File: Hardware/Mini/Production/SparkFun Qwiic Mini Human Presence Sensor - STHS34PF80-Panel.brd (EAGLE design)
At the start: 175 x 93 mm, 1410 parts, among them J1 Qwiic, J10 Qwiic, J100 Qwiic, J101 Qwiic, J103 Qwiic, J104 Qwiic, J106 Qwiic, J107 Qwiic, J11 Qwiic, J13 Qwiic, J14 Qwiic, J16 Qwiic, J17 Qwiic, J19 Qwiic, J2 Qwiic, J20 Qwiic, J22 Qwiic, J23 Qwiic, J25 Qwiic, J26 Qwiic, J28 Qwiic, J29 Qwiic, J31 Qwiic, J32 Qwiic, J34 Qwiic, J35 Qwiic, J37 Qwiic, J38 Qwiic, J4 Qwiic, J40 Qwiic, J41 Qwiic, J43 Qwiic, J44 Qwiic, J46 Qwiic, J47 Qwiic, J49 Qwiic, J5 Qwiic, J50 Qwiic, J52 Qwiic, J53 Qwiic, J55 Qwiic, J56 Qwiic, J58 Qwiic, J59 Qwiic, J61 Qwiic, J62 Qwiic, J64 Qwiic, J65 Qwiic, J67 Qwiic, J68 Qwiic, J7 Qwiic, J70 Qwiic, J71 Qwiic, J73 Qwiic, J74 Qwiic, J76 Qwiic, J77 Qwiic, J79 Qwiic, J8 Qwiic, J80 Qwiic, J82 Qwiic, J83 Qwiic, J85 Qwiic, J86 Qwiic, J88 Qwiic, J89 Qwiic, J91 Qwiic, J92 Qwiic, J94 Qwiic, J95 Qwiic, J97 Qwiic, J98 Qwiic, U1 STHS34PF80, U10 STHS34PF80, U11 STHS34PF80, U12 STHS34PF80, U13 STHS34PF80, U14 STHS34PF80, U15 STHS34PF80, U16 STHS34PF80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

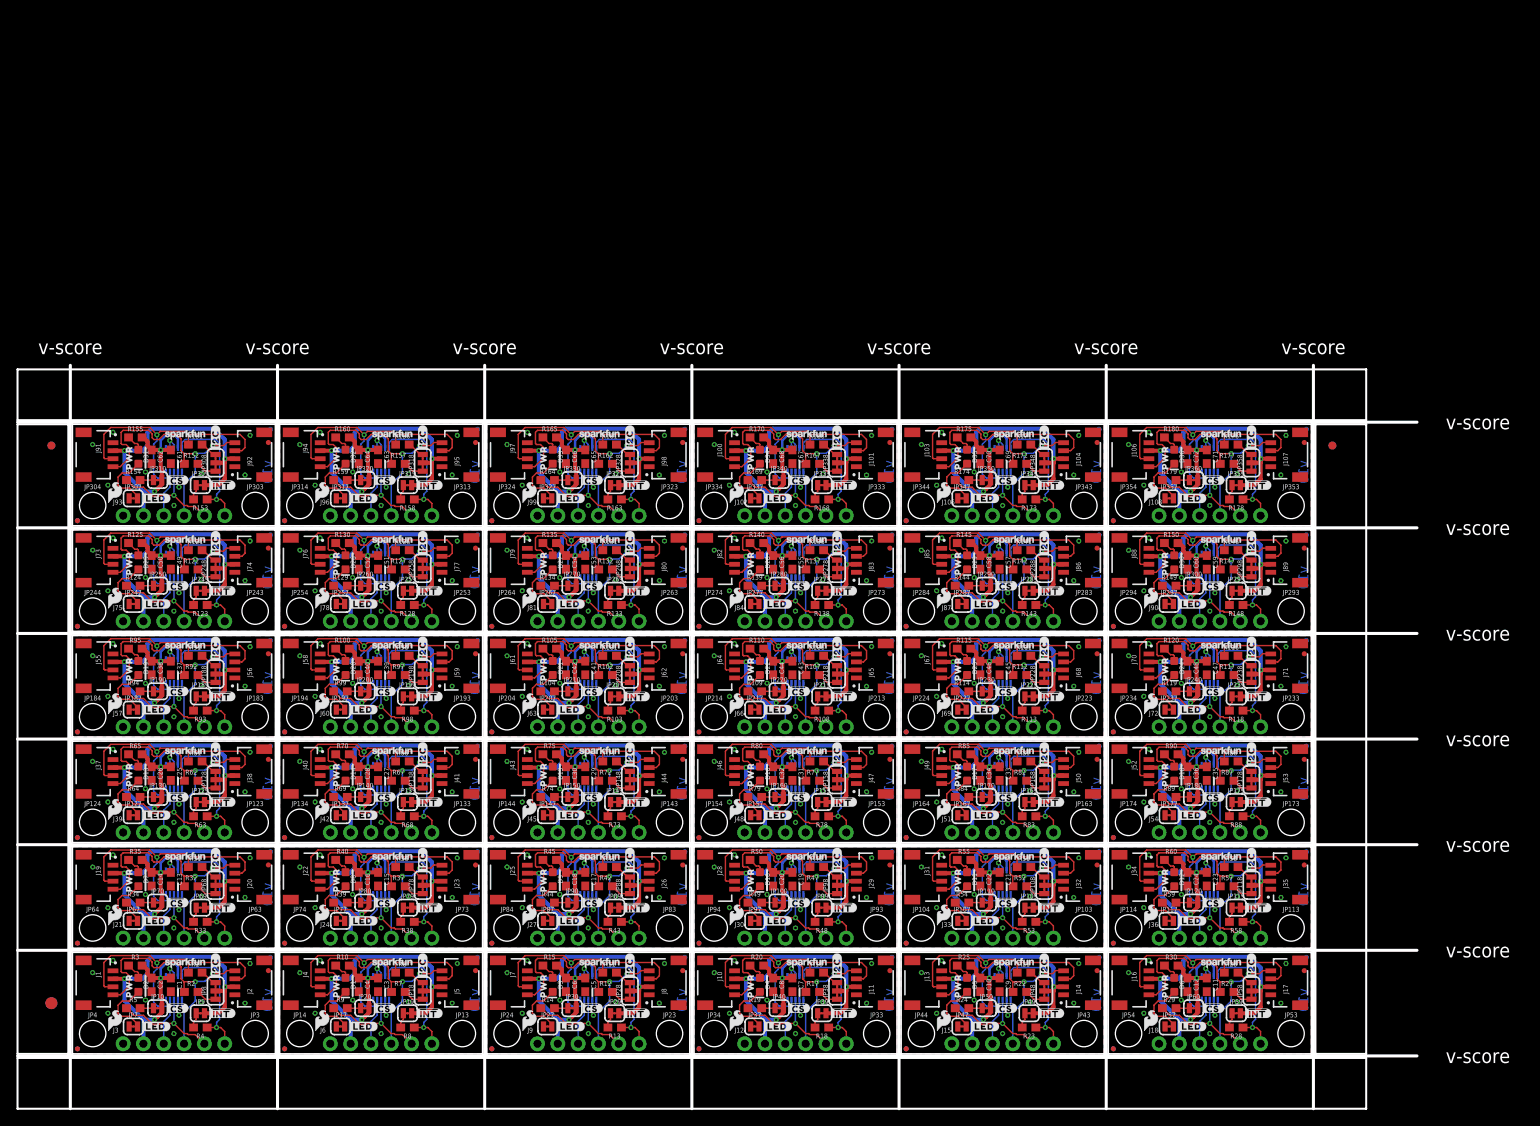
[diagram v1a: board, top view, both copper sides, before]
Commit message: Changed from Qwiic horizontal to qwiic vertical
Changed to the Qwiic Vertical connector we have for a better surface mounting option for the user. Updated the gerbers and panel to now have the correct information
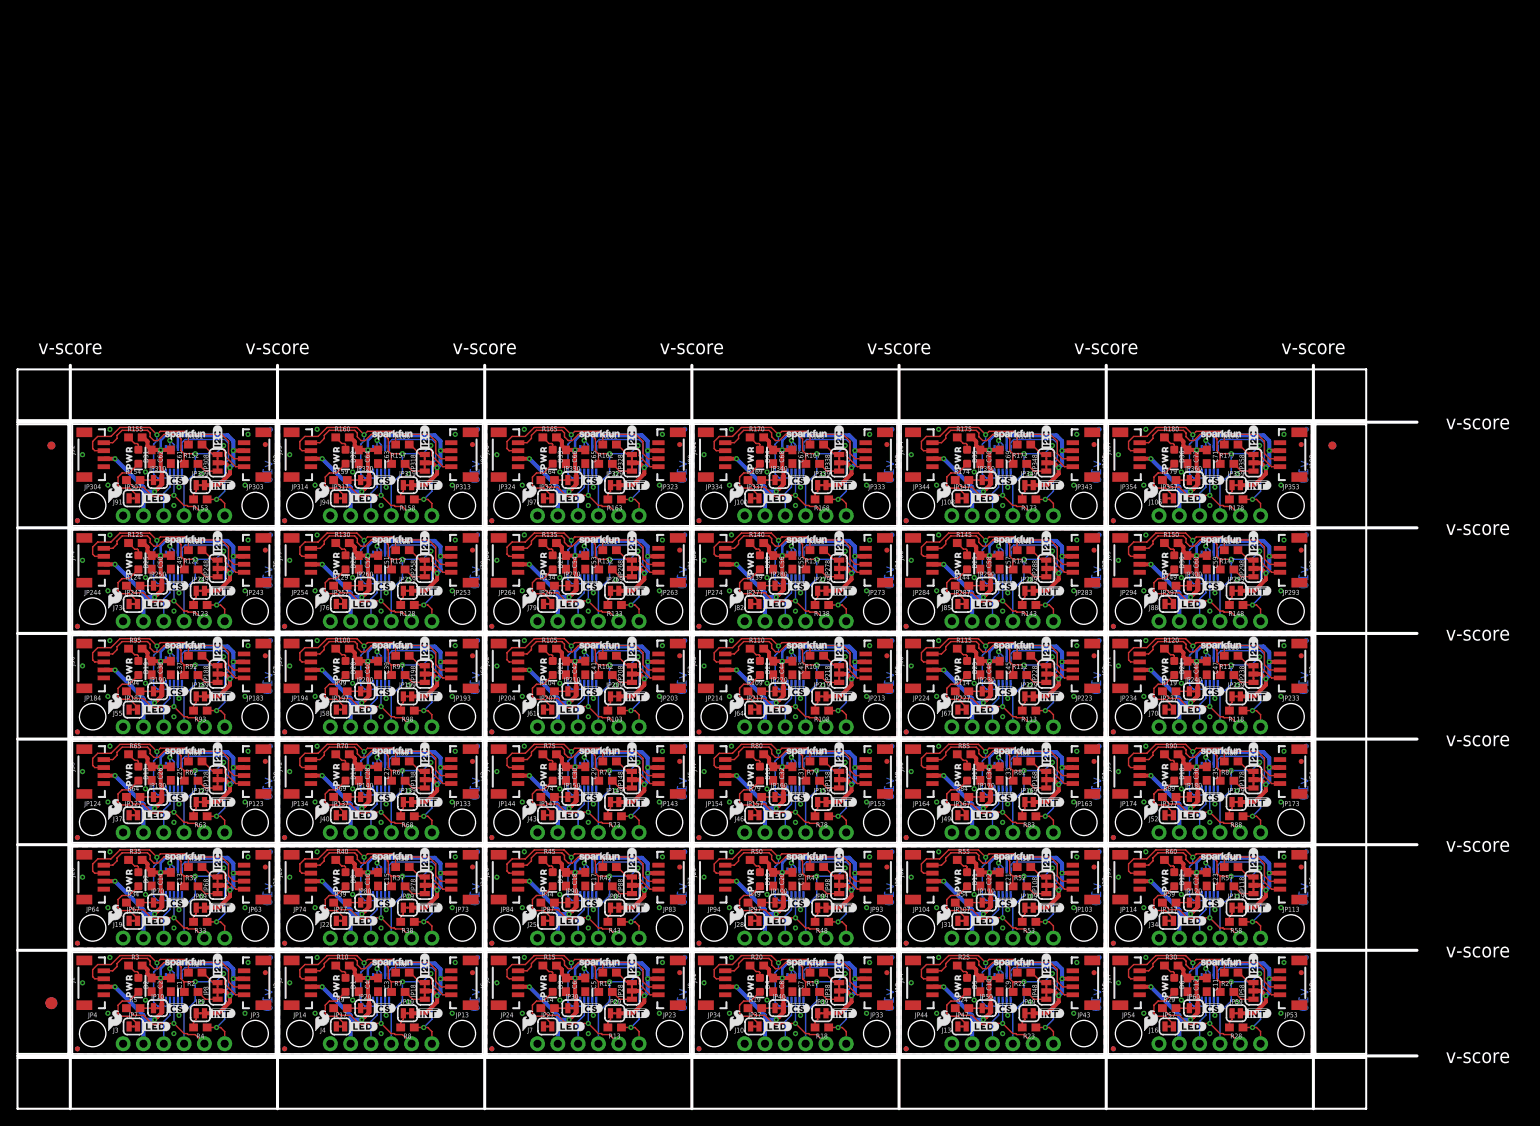
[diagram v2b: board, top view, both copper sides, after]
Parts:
- J1, J101, J104, J107, J11, J14, J17, J2, J20, J23, J26, J29, J32, J35, J38, J41, J44, J47, J5, J50, J53, J56, J59, J62, J65, J68, J71, J74, J77, J8, J80, J83, J86, J89, J92, J95, J98: value Qwiic -> Vertical Qwiic Connector; device SparkFun-Connectors:JST04_1MM_RA -> SparkFun-Connectors:JST04_1MM_VERT
- J10, J100, J103, J106, J13, J16, J19, J22, J25, J28, J31, J34, J37, J4, J40, J43, J46, J49, J52, J55, J58, J61, J64, J67, J7, J70, J73, J76, J79, J82, J85, J88, J91, J94, J97: value Qwiic -> (none); device SparkFun-Connectors:JST04_1MM_RA -> SparkFun-Connectors:1X06_NO_SILK
- J102, J105, J108, J12, J15, J18, J21, J24, J27, J30, J33, J36, J39, J42, J45, J48, J51, J54, J57, J6, J60, J63, J66, J69, J72, J75, J78, J81, J84, J87, J9, J90, J93, J96, J99: value (none) -> Vertical Qwiic Connector; device SparkFun-Connectors:1X06_NO_SILK -> SparkFun-Connectors:JST04_1MM_VERT
- moved J108 16.2 mm to (150.2, 74.9), turned to 270 degrees
- moved J72 16.2 mm to (150.2, 48.5), turned to 270 degrees
- moved J90 16.2 mm to (150.2, 61.7), turned to 270 degrees
- moved J18 16.2 mm to (150.2, 8.89), turned to 270 degrees
- moved J36 16.2 mm to (150.2, 22.1), turned to 270 degrees
- moved J54 16.2 mm to (150.2, 35.3), turned to 270 degrees
- moved J57 16.2 mm to (20.7, 48.5), turned to 270 degrees
- moved J75 16.2 mm to (20.7, 61.7), turned to 270 degrees
- moved J93 16.2 mm to (20.7, 74.9), turned to 270 degrees
- moved J102 16.2 mm to (98.4, 74.9), turned to 270 degrees
- moved J105 16.2 mm to (124.3, 74.9), turned to 270 degrees
- moved J12 16.2 mm to (98.4, 8.89), turned to 270 degrees
- moved J15 16.2 mm to (124.3, 8.89), turned to 270 degrees
- moved J21 16.2 mm to (20.7, 22.1), turned to 270 degrees
- moved J24 16.2 mm to (46.6, 22.1), turned to 270 degrees
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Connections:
- net !CS!1: now also J4.5; no longer J6.5
- net !CS!10: now also J31.5; no longer J33.5
- net !CS!11: now also J34.5; no longer J36.5
- net !CS!12: now also J37.5; no longer J39.5
- net !CS!13: now also J40.5; no longer J42.5
- net !CS!14: now also J43.5; no longer J45.5
- net !CS!15: now also J46.5; no longer J48.5
- net !CS!16: now also J49.5; no longer J51.5
- net !CS!17: now also J52.5; no longer J54.5
- net !CS!18: now also J55.5; no longer J57.5
- net !CS!19: now also J58.5; no longer J60.5
- net !CS!2: now also J7.5; no longer J9.5
- net !CS!20: now also J61.5; no longer J63.5
- net !CS!21: now also J64.5; no longer J66.5
- net !CS!22: now also J67.5; no longer J69.5
- net !CS!23: now also J70.5; no longer J72.5
- net !CS!24: now also J73.5; no longer J75.5
- net !CS!25: now also J76.5; no longer J78.5
- net !CS!26: now also J79.5; no longer J81.5
- net !CS!27: now also J82.5; no longer J84.5
- net !CS!28: now also J85.5; no longer J87.5
- net !CS!29: now also J88.5; no longer J90.5
- net !CS!3: now also J10.5; no longer J12.5
- net !CS!30: now also J91.5; no longer J93.5
- net !CS!31: now also J94.5; no longer J96.5
- net !CS!32: now also J97.5; no longer J99.5
- net !CS!33: now also J100.5; no longer J102.5
- net !CS!34: now also J103.5; no longer J105.5
- net !CS!35: now also J106.5; no longer J108.5
- net !CS!4: now also J13.5; no longer J15.5
- net !CS!5: now also J16.5; no longer J18.5
- net !CS!6: now also J19.5; no longer J21.5
- net !CS!7: now also J22.5; no longer J24.5
- net !CS!8: now also J25.5; no longer J27.5
- net !CS!9: now also J28.5; no longer J30.5
- net INT1: now also J4.6; no longer J6.6
- net INT10: now also J31.6; no longer J33.6
- net INT11: now also J34.6; no longer J36.6
- net INT12: now also J37.6; no longer J39.6
- net INT13: now also J40.6; no longer J42.6
- net INT14: now also J43.6; no longer J45.6
- net INT15: now also J46.6; no longer J48.6
- net INT16: now also J49.6; no longer J51.6
- net INT17: now also J52.6; no longer J54.6
- net INT18: now also J55.6; no longer J57.6
- net INT19: now also J58.6; no longer J60.6
- net INT2: now also J7.6; no longer J9.6
- net INT20: now also J61.6; no longer J63.6
- net INT21: now also J64.6; no longer J66.6
- net INT22: now also J67.6; no longer J69.6
- net INT23: now also J70.6; no longer J72.6
- net INT24: now also J73.6; no longer J75.6
- net INT25: now also J76.6; no longer J78.6
- net INT26: now also J79.6; no longer J81.6
- net INT27: now also J82.6; no longer J84.6
- net INT28: now also J85.6; no longer J87.6
- net INT29: now also J88.6; no longer J90.6
- net INT3: now also J10.6; no longer J12.6
- net INT30: now also J91.6; no longer J93.6
- net INT31: now also J94.6; no longer J96.6
- net INT32: now also J97.6; no longer J99.6
- net INT33: now also J100.6; no longer J102.6
- net INT34: now also J103.6; no longer J105.6
- net INT35: now also J106.6; no longer J108.6
- net INT4: now also J13.6; no longer J15.6
- net INT5: now also J16.6; no longer J18.6
- net INT6: now also J19.6; no longer J21.6
- net INT7: now also J22.6; no longer J24.6
- net INT8: now also J25.6; no longer J27.6
- net INT9: now also J28.6; no longer J30.6
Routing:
- net 3.3V35: track 54.0 -> 46.2 mm, vias 4 -> 5
- net 3.3V5: track 54.0 -> 46.2 mm, vias 4 -> 5
- net 3.3V29: track 54.0 -> 46.2 mm, vias 4 -> 5
- net 3.3V17: track 54.0 -> 46.2 mm, vias 4 -> 5
- net 3.3V25: track 54.0 -> 46.2 mm, vias 4 -> 5
- net 3.3V23: track 54.0 -> 46.2 mm, vias 4 -> 5
- net 3.3V: track 54.0 -> 46.2 mm, vias 4 -> 5
- net 3.3V33: track 54.0 -> 46.2 mm, vias 4 -> 5
- net 3.3V31: track 54.0 -> 46.2 mm, vias 4 -> 5
- net 3.3V3: track 54.0 -> 46.2 mm, vias 4 -> 5
- net 3.3V27: track 54.0 -> 46.2 mm, vias 4 -> 5
- net 3.3V21: track 54.0 -> 46.2 mm, vias 4 -> 5
- net 3.3V19: track 54.0 -> 46.2 mm, vias 4 -> 5
- net 3.3V15: track 54.0 -> 46.2 mm, vias 4 -> 5
- net 3.3V14: track 54.0 -> 46.2 mm, vias 4 -> 5
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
